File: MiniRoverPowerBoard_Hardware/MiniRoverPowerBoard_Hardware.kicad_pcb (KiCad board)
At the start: 2 copper layers, 68 parts, among them Q1 Q_NMOS_GSD, Q2 Q_NMOS_GSD, Q3 Q_PMOS_GDS, Q4 Q_NMOS_GSD, SW1 Relay_SPST, SW2 SW_Push, SW3 SW_Push, SW4 SW_SPDT, U1 VNH5019A_E, U2 VNH5019A_E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

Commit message: Almost All Components Layed Out
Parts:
- removed R15: 10k, Resistor_SMD:R_0603_1608Metric_Pad1.05x0.95mm_HandSolder
- removed SW4: SW_SPDT, Button_Switch_THT:SW_CuK_OS102011MA1QN1_SPDT_Angled
- added C10: 10u, Capacitor_SMD:C_0603_1608Metric_Pad1.05x0.95mm_HandSolder, F.Cu at (206.4, 62.2)
- added C11: 10u, Capacitor_SMD:C_0603_1608Metric_Pad1.05x0.95mm_HandSolder, F.Cu at (209.7, 60.7)
- added C12: 10u, Capacitor_SMD:C_0603_1608Metric_Pad1.05x0.95mm_HandSolder, F.Cu at (209.7, 62.2)
- added C9: 10u, Capacitor_SMD:C_0603_1608Metric_Pad1.05x0.95mm_HandSolder, F.Cu at (206.4, 60.7)
- moved L1 172.0 mm to (137.2, 123.2), turned to 90 degrees
- moved L2 154.2 mm to (148.6, 123.2), turned to 90 degrees
- moved Conn2 151.7 mm to (166.4, 119.4), turned to 180 degrees
- moved Conn3 136.8 mm to (135.9, 49.5)
- moved Conn4 134.7 mm to (166.4, 33.8), turned to 180 degrees
- moved Conn6 128.0 mm to (146.1, 133.3)
- moved R22 126.3 mm to (121.3, 67.8), turned to 180 degrees
- moved R13 118.6 mm to (119.4, 63.5), turned to 180 degrees
- moved R9 118.5 mm to (153.0, 113.0)
- moved C4 118.2 mm to (144.8, 116.2)
- moved C5 117.4 mm to (149.2, 57.1)
- moved C7 116.6 mm to (136.5, 116.2)
- moved Conn1 116.6 mm to (166.4, 102.9), turned to 180 degrees
- moved C6 116.6 mm to (149.2, 67.3)
- moved R10 116.4 mm to (143.5, 106.0), turned to 180 degrees
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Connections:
- Conn3 pad 1: OUT_B_LEFT -> OUT_A_LEFT
- Conn3 pad 2: OUT_A_LEFT -> OUT_B_LEFT
- Conn4 pad 1: OUT_B_RIGHT -> OUT_A_RIGHT
- Conn4 pad 2: OUT_A_RIGHT -> OUT_B_RIGHT
- SW1 pad 2: /PVDD_IN3 -> +5V
- U6 pad 4: DIRECTION_SW -> LOG_SW_EN
- U6 pad RX: LOG_SW_EN -> Net-(U6-PadRX)
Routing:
- added copper zone on B.Cu, net GND
- added copper zone on F.Cu, net GND
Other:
- board outline added: 78.7 x 104.1 mm

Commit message: All Comps Placed; Adding more though :(
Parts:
- moved C11 87.6 mm to (122.2, 63.5), turned to 180 degrees
- moved R18 81.7 mm to (136.4, 111.5)
- moved D4 76.5 mm to (140.5, 111.5), turned to 180 degrees
- moved R17 69.2 mm to (144.5, 111.5)
- moved D3 63.6 mm to (148.8, 111.5), turned to 180 degrees
- moved C10 59.6 mm to (146.8, 62.2), turned to 180 degrees
- moved R16 58.1 mm to (148.8, 51.3)
- moved D2 56.4 mm to (153.2, 51.3), turned to 180 degrees
- moved C12 54.6 mm to (155.2, 62.2)
- moved R12 47.7 mm to (176.3, 77.2)
- moved R11 43.2 mm to (176.3, 80.3)
- moved Q3 39.9 mm to (182.6, 75.4), turned to 90 degrees
- moved C9 26.5 mm to (180.1, 63.5)
- moved U3 23.9 mm to (182.6, 87.6), turned to 180 degrees
- moved F1 22.7 mm to (188.0, 94.5), turned to 180 degrees
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
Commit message: Added Extra Buses & Started Polygons
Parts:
- added Conn10: Molex_SL_04, MRDT_Connectors:MOLEX_SL_04_Vertical, F.Cu at (150.6, 91.7)
- added Conn7: Molex_SL_02, MRDT_Connectors:MOLEX_SL_02_Vertical, F.Cu at (139.2, 82.0)
- added Conn8: Molex_SL_02, MRDT_Connectors:MOLEX_SL_02_Vertical, F.Cu at (139.2, 91.7)
- added Conn9: Molex_SL_04, MRDT_Connectors:MOLEX_SL_04_Vertical, F.Cu at (150.6, 82.0)
- added G***: LOGO, MRDT_Silkscreens:0_MRDT_Logo_20mm, F.Cu at (168.9, 82.8)
- added R15: 0, Resistor_SMD:R_0603_1608Metric_Pad1.05x0.95mm_HandSolder, F.Cu at (130.8, 85.3)
- added R26: 0, Resistor_SMD:R_0603_1608Metric_Pad1.05x0.95mm_HandSolder, F.Cu at (130.8, 82.5)
- added R27: 0, Resistor_SMD:R_0603_1608Metric_Pad1.05x0.95mm_HandSolder, F.Cu at (133.3, 83.8)
- moved D9 53.3 mm to (160.8, 100.1), turned to 0 degrees
- moved R23 48.5 mm to (162.3, 96.8), turned to 90 degrees
- moved R22 47.8 mm to (159.3, 96.8), turned to 270 degrees
- moved Q4 19.4 mm to (117.3, 69.8), turned to 180 degrees
- moved R25 17.8 mm to (123.2, 69.8)
- moved B1 13.0 mm to (128.8, 79.8), turned to 180 degrees
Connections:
- U6 pad RX: Net-(U6-PadRX) -> RX
- U6 pad TX: Net-(U6-PadTX) -> TX
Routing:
- added copper zone on F.Cu, net /PVDD_IN1
- added copper zone on F.Cu, net /PVDD_IN2
- added copper zone on F.Cu, net /PVDD_IN3
- added copper zone on B.Cu, net ACT_PWR
- added copper zone on F.Cu, net ACT_PWR
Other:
- board text added: "+"
- board text added: "-"
- board text added: "30A"

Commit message: Majority of routing complete; few buses to go
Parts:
- moved G*** 40.8 mm to (206.0, 65.8)
- moved R10 6.35 mm to (137.2, 106.2)
- moved D9 5.61 mm to (160.3, 94.5)
- moved R22 5.61 mm to (158.8, 91.2)
- moved R23 5.61 mm to (161.8, 91.2)
- moved Q2 4.95 mm to (142.7, 106.0), turned to 0 degrees
- moved D1 4.45 mm to (152.4, 110.7)
- moved R9 2.93 mm to (156.0, 112.3)
- moved R8 2.92 mm to (156.0, 109.2)
- moved C5 2.82 mm to (150.9, 59.4), turned to 90 degrees
- moved C6 2.08 mm to (150.9, 66.0), turned to 270 degrees
- moved R12 1.78 mm to (176.3, 79.0)
- moved R11 1.52 mm to (176.3, 81.8)
- moved R6 1.14 mm to (170.9, 73.0)
- moved C10 0.51 mm to (146.8, 62.7)
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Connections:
- U6 pad 10: IN_B1 -> IN_B2
- U6 pad 11: IN_A2 -> RIGHT_SW
- U6 pad 12: IN_B2 -> LEFT_SW
- U6 pad 2: LEFT_SW -> BUZZER_EN
- U6 pad 3: RIGHT_SW -> ESTOP_EN
- U6 pad 5: LEFT_PWM -> IN_A1
- U6 pad 6: RIGHT_PWM -> LEFT_PWM
- U6 pad 7: ESTOP_EN -> IN_B1
- U6 pad 8: BUZZER_EN -> IN_A2
- U6 pad 9: IN_A1 -> RIGHT_PWM
- U6 pad A3: PACK_IMEAS -> V_LOG_SENSE
- U6 pad A4: V_LOG_SENSE -> PACK_IMEAS
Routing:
- net +5V: track 0.00 -> 212.0 mm, vias 0 -> 7
- net +3V3: track 0.00 -> 137.7 mm, vias 0 -> 10
- net RIGHT_SW: track 0.00 -> 134.8 mm
- net IN_B2: track 0.00 -> 103.5 mm
- net RIGHT_PWM: track 0.00 -> 97.8 mm
- net IN_A2: track 0.00 -> 89.3 mm
- net LEFT_SW: track 0.00 -> 82.8 mm
- net IN_B1: track 0.00 -> 68.5 mm
- net ACT_PWR: track 0.00 -> 66.1 mm, vias 0 -> 183
- net LEFT_PWM: track 0.00 -> 61.4 mm
- net Net-(Q2-Pad3): track 0.00 -> 54.2 mm
- net IN_A1: track 0.00 -> 52.5 mm
- net /PVDD_IN3: track 0.00 -> 48.0 mm
- net CONTROLLER_DAT: track 0.00 -> 47.3 mm
- net BUZZER_EN: track 0.00 -> 41.4 mm
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- added copper zone on B.Cu, net OUT_A_LEFT
- added copper zone on F.Cu, net OUT_A_LEFT
- added copper zone on B.Cu, net OUT_A_RIGHT
- added copper zone on F.Cu, net OUT_A_RIGHT
- added copper zone on B.Cu, net OUT_B_LEFT
- added copper zone on F.Cu, net OUT_B_LEFT
- added copper zone on B.Cu, net OUT_B_RIGHT
- added copper zone on F.Cu, net OUT_B_RIGHT

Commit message: Layout & silkscreen complete; Ready for review
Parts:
- added G***: LOGO, MRDT_Silkscreens:z_sig_Jacob_Lipina_Sig_15mm, F.Cu at (133.3, 139.7)
- added G***: LOGO, MRDT_Silkscreens:2_Meh, B.Cu at (173.1, 136.1)
- added G***: LOGO, MRDT_Silkscreens:2_Nothing_3mm_Cu, F.Cu at (156.6, 27.9)
- added G***: LOGO, MRDT_Silkscreens:0_MRDT_Logo_7.5mm, F.Cu at (137.3, 28.7)
- added G***: LOGO, MRDT_Silkscreens:2_Dahlbot_2.0, F.Cu at (123.2, 122.7)
- added G***: LOGO, MRDT_Silkscreens:0_MRDT_Retro_Logo_40mmX25.3mm, B.Cu at (151.3, 63.5)
- added REF**: 4_40_Hole, MRDT_Drill_Holes:4_40_Hole, F.Cu at (115.6, 29.2)
- added REF**: 4_40_Hole, MRDT_Drill_Holes:4_40_Hole, F.Cu at (186.7, 29.2)
- added REF**: 4_40_Hole, MRDT_Drill_Holes:4_40_Hole, F.Cu at (186.7, 139.7)
- added REF**: 4_40_Hole, MRDT_Drill_Holes:4_40_Hole, F.Cu at (115.6, 139.7)
- moved G*** 42.1 mm to (167.6, 83.1)
- moved R22 38.4 mm to (188.5, 66.8)
- moved D9 34.2 mm to (188.5, 75.2), turned to 90 degrees
- moved R23 33.7 mm to (188.5, 70.6), turned to 270 degrees
- moved D11 1.80 mm to (154.2, 39.5)
- moved R24 1.80 mm to (157.2, 39.5)
- moved D5 1.78 mm to (147.8, 39.5)
- moved R19 1.78 mm to (144.8, 39.5)
- moved D2 1.27 mm to (153.2, 50.5)
- moved R16 1.27 mm to (148.8, 50.5)
- moved Q2 0.38 mm to (142.7, 105.7)
- turned R14 to 0 degrees
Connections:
- U6 pad A4: PACK_IMEAS -> V_ACT_SENSE
- U6 pad A5: V_ACT_SENSE -> PACK_IMEAS
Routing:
- net V_ACT_SENSE: track 5.53 -> 163.4 mm, vias 0 -> 2
- net PACK_IMEAS: track 0.00 -> 150.1 mm, vias 0 -> 2
- net LOGIC_PWR: track 39.1 -> 114.4 mm, vias 3 -> 5
- net LOG_SW_EN: track 40.2 -> 81.7 mm
- net ESTOP_EN: track 35.8 -> 56.4 mm
- net ACT_PWR: track 66.1 -> 60.2 mm, vias 183 -> 181
- net +5V: track 212.0 -> 210.5 mm
- net CONTROLLER_DAT: track 47.3 -> 46.2 mm
- net CONTROLLER_CMD: track 32.0 -> 31.0 mm
- net CONTROLLER_ATT: track 39.7 -> 38.7 mm
- net OUT_B_RIGHT: track 21.0 -> 22.0 mm
- net OUT_A_LEFT: track 21.1 -> 21.8 mm
- net +3V3: track 137.7 -> 138.4 mm
- net GND: vias 95 -> 114
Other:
- board size 78.7 x 104.1 mm -> 78.7 x 118.1 mm
- board text added: "#R VESOHARD"
- board text added: "+VI"
- board text added: "12V EXTRA 1"
- board text added: "12V EXTRA 2"
- board text added: "3.3V"
- board text added: "3.3V PWR"
- board text added: "35A"
- board text added: "4-40"
- board text added: "5+"
- board text added: "5V"
- board text added: "5V EXTRA"
- board text added: "5V PWR"
- board text added: "ACT PWR"
- board text added: "ATT"
- board text added: "CLK"
- board text added: "CMD"
- board text added: "COIL OUT"
- board text added: "CONTROLLER RECEIVER"
- board text added: "DAT"
- board text added: "E-STOP"
- board text added: "LEFT"
- board text added: "LOG PWR"
- board text added: "LOGIC SWITCH"
- board text added: "MOTOR OUTPUTS"
- board text added: "Mini Rover Power Board Rev. 1 Missouri S&T MRDT, 2019 Jacob Lipina"
- board text added: "NC"
- board text added: "OUT_A"
- board text added: "OUT_B"
- board text added: "PVDD"
- board text added: "RIGHT"
- board text added: "RX"
- board text added: "Run Left Motors"
- board text added: "Run Right Motors"
- board text added: "SERIAL"
- board text added: "TX"
- board text removed: "30A"

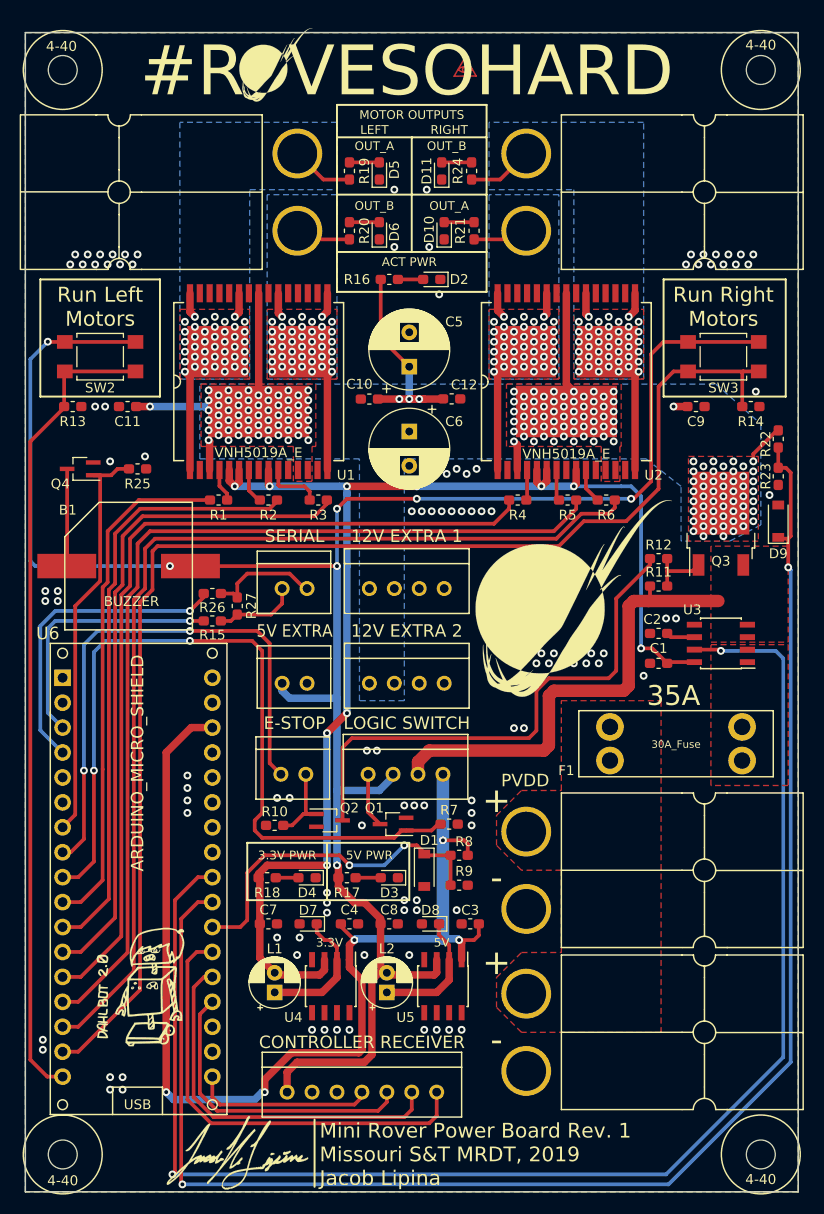
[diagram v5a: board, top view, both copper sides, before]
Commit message: Removed 3v3 AP1509 and changed voltage dividers
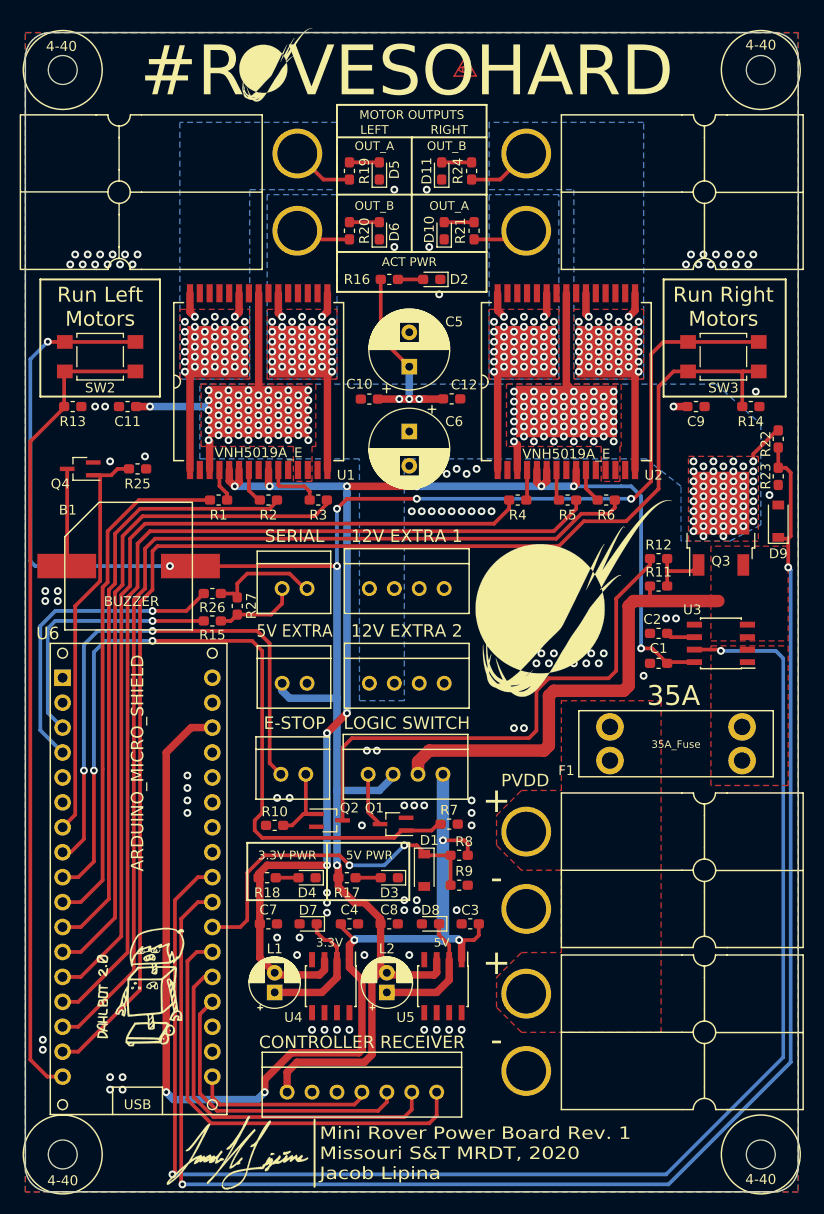
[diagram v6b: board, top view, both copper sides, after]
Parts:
- F1: value 30A_Fuse -> 35A_Fuse
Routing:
- net +5V: track 210.5 -> 211.4 mm
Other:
- outline, holes or cut-outs redrawn
- board text added: "Mini Rover Power Board Rev. 1 Missouri S&T MRDT, 2020 Jacob Lipina"
- board text removed: "Mini Rover Power Board Rev. 1 Missouri S&T MRDT, 2019 Jacob Lipina"

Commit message: Finished board changes for arduino pwr & added gerbs
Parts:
- removed C3, C7: 10u, Capacitor_SMD:C_0603_1608Metric_Pad1.05x0.95mm_HandSolder
- removed D7: D_Schottky, Diode_SMD:D_0603_1608Metric_Pad1.05x0.95mm_HandSolder
- removed L1: 47uH, Capacitor_THT:CP_Radial_D5.0mm_P2.00mm
- removed R27: 0, Resistor_SMD:R_0603_1608Metric_Pad1.05x0.95mm_HandSolder
- removed U4: AP1509, Package_SO:SOIC-8_3.9x4.9mm_P1.27mm
- Conn7: value Molex_SL_02 -> Molex_SL_03; footprint MRDT_Connectors:MOLEX_SL_02_Vertical -> MRDT_Connectors:MOLEX_SL_03_Vertical
- D1, D9: value 3V3_Zener -> 4.7V_Zener
- R22, R8: value 20k -> 21k
- R23, R9: value 13k -> 26.7k
- moved R26 20.7 mm to (133.7, 103.0), turned to 270 degrees
- moved R15 11.6 mm to (127.0, 96.3)
- moved C4 8.38 mm to (153.2, 116.2)
- moved L2 5.59 mm to (143.0, 122.9)
- moved U5 5.59 mm to (148.7, 122.3)
- moved C8 4.06 mm to (144.8, 116.2)
- moved D8 4.06 mm to (149.0, 116.2)
- moved Conn10 3.81 mm to (146.8, 91.7)
- moved Conn7 3.81 mm to (135.4, 82.0)
- moved Conn9 3.81 mm to (146.8, 82.0)
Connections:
- Conn7 pad 1: Net-(Conn7-Pad1) -> TX
- Conn7 pad 2: Net-(Conn7-Pad2) -> RX
- R15 pad 1: Net-(Conn7-Pad1) -> /VIN_R
- R15 pad 2: TX -> LOGIC_PWR
- R26 pad 1: Net-(Conn7-Pad2) -> /5V_R
- R26 pad 2: RX -> +5V
- U6 pad 3.3V: Net-(U6-Pad3.3V) -> +3V3
- U6 pad 5V: Net-(U6-Pad5V) -> /5V_R
- U6 pad VI: LOGIC_PWR -> /VIN_R
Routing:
- net LOGIC_PWR: track 114.4 -> 95.4 mm, vias 5 -> 4
- net Net-(D7-Pad1): track 13.6 -> 0.00 mm
- net Net-(Conn7-Pad2): track 11.4 -> 0.00 mm
- net RX: track 31.9 -> 41.2 mm
- net TX: track 26.9 -> 35.7 mm, vias 1 -> 2
- net Net-(Conn7-Pad1): track 8.50 -> 0.00 mm
- net +3V3: track 138.4 -> 143.6 mm
- net /5V_R: track 0.00 -> 3.63 mm
- net +5V: track 211.4 -> 214.7 mm, vias 7 -> 11
- net /VIN_R: track 0.00 -> 2.96 mm
- net Net-(D8-Pad1): track 13.0 -> 12.2 mm
- net LOG_SW_EN: track 81.7 -> 81.6 mm, vias 2 -> 4
- net GND: vias 114 -> 123
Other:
- board text added: "3V3"
- board text removed: "3.3V"
